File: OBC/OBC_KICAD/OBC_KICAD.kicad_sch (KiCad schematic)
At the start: 0 parts

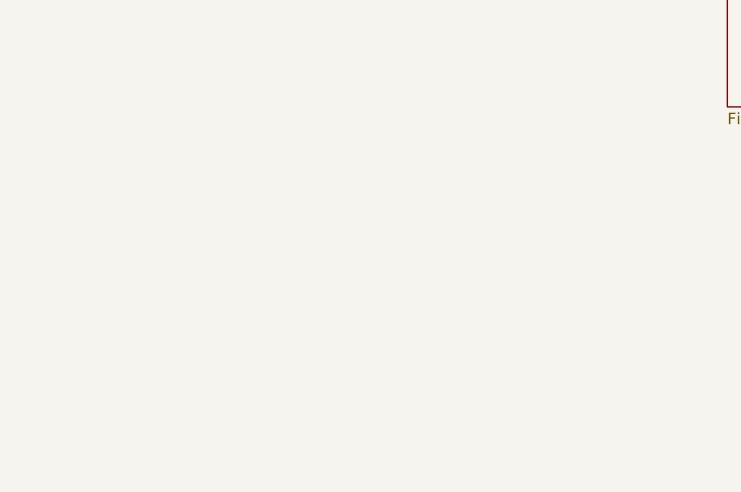
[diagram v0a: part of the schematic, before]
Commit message: Agregar OCP TPS2052BDR y Watchdog STWD100
Agregue un OCP y un WatchDOg ,todo en la HOja con NOmbre Wtachdog.
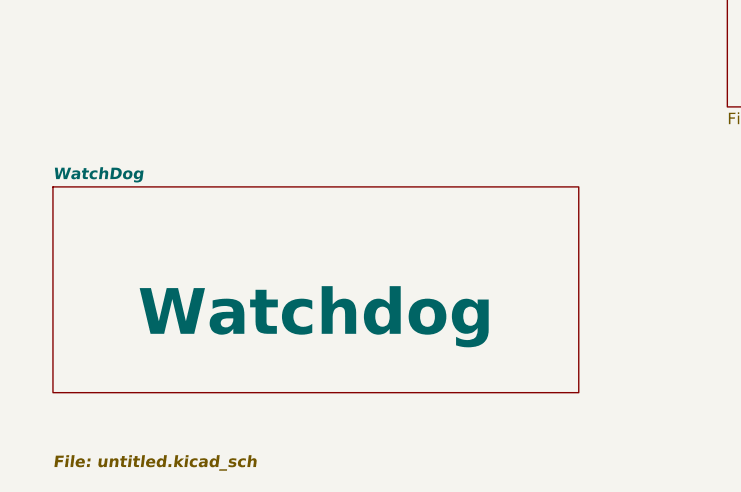
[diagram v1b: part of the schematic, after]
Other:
- added sheet WatchDog (untitled.kicad_sch)
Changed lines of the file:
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@@
+	)
+	(sheet
+		(at 62.23 116.84)
+		(size 58.42 22.86)
+		(exclude_from_sim no)
+		(in_bom yes)
+		(on_board yes)
+		(dnp no)
+		(stroke
+			(width 0.1524)
+			(type solid)
+		)
+		(fill
+			(color 0 0 0 0.0000)
+		)
+		(property "Sheetname" "WatchDog"
+			(at 62.23 116.1284 0)
+			(show_name yes)
+			(effects
+				(font
+					(size 1.27 1.27)
+					(thickness 0.254)
+					(bold yes)
+					(italic yes)
+				)
+				(justify left bottom)
+			)
+		)
+		(property "Sheetfile" "untitled.kicad_sch"
+			(at 62.23 146.6346 0)
+			(show_name yes)
+			(effects
+				(font
+					(size 1.27 1.27)
+					(thickness 0.254)
+					(bold yes)
+					(italic yes)
+				)
+				(justify left top)
+			)
+		)
+		(property "WatchDog" "Watchdog"
+			(at 91.44 130.81 0)
+			(effects
+				(font
+					(size 5.08 5.08)
+					(thickness 1.016)
+					(bold yes)
+				)
+			)
+		)
+		(instances
+			(project "OBC_KICAD"
+				(path "/6db8dc25-5ab8-4f32-8d05-e8d57edb0b6f"
+					(page "4")
+				)
+			)
+		)
 	)
 	(sheet

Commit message: Cirtcuito Completo
Circuito Completo
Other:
- added sheet Pines de Entrada y Salida Al circuito (Pines de Interfaz.kicad_sch)
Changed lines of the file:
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@@
 	(text "JST \nSWD\nUSB"
 		(exclude_from_sim no)
-		(at 166.37 77.47 0)
+		(at 137.16 49.53 0)
 		(effects
 			(font
@@
 	(text "MCU"
 		(exclude_from_sim no)
-		(at 83.058 77.47 0)
+		(at 53.848 49.53 0)
 		(effects
 			(font
@@
 	)
 	(sheet
-		(at 58.42 59.69)
+		(at 29.21 31.75)
 		(size 50.8 30.48)
 		(exclude_from_sim no)
@@
 		)
 		(property "Sheetname" "Microcontrolador"
-			(at 58.42 58.9784 0)
+			(at 29.21 31.0384 0)
 			(effects
 				(font
@@
 		)
 		(property "Sheetfile" "microcontrolador.kicad_sch"
-			(at 58.42 90.7546 0)
+			(at 29.21 62.8146 0)
 			(effects
 				(font
@@
 	)
 	(sheet
-		(at 62.23 116.84)
-		(size 58.42 22.86)
+		(at 19.05 85.09)
+		(size 85.09 26.67)
 		(exclude_from_sim no)
 		(in_bom yes)
@@
 		)
 		(property "Sheetname" "WatchDog"
-			(at 62.23 116.1284 0)
+			(at 19.05 84.3784 0)
 			(show_name yes)
 			(effects
@@
 		)
 		(property "Sheetfile" "untitled.kicad_sch"
-			(at 62.23 146.6346 0)
+			(at 19.05 114.8846 0)
 			(show_name yes)
 			(effects
@@
 			)
 		)
-		(property "WatchDog" "Watchdog"
-			(at 91.44 130.81 0)
+		(property "WatchDog" "    Watchdog n' OCP"
+			(at 48.26 99.06 0)
 			(effects
 				(font
@@
 	)
 	(sheet
-		(at 137.16 44.45)
+		(at 144.78 93.98)
+		(size 106.68 38.1)
+		(exclude_from_sim no)
+		(in_bom yes)
+		(on_board yes)
+		(dnp no)
+		(stroke
+			(width 0.1524)
+			(type solid)
+		)
+		(fill
+			(color 0 0 0 0.0000)
+		)
+		(property "Sheetname" "Pines de Entrada y Salida Al circuito"
+			(at 144.78 93.2684 0)
+			(effects
+				(font
+					(size 1.27 1.27)
+				)
+				(justify left bottom)
+			)
+		)
+		(property "Sheetfile" "Pines de Interfaz.kicad_sch"
+			(at 144.78 128.8546 0)
+			(effects
+				(font
+					(size 1.27 1.27)
+				)
+				(justify left top)
+			)
+		)
+		(property "Field2" "             Pines de Interfaz"
+			(at 180.848 108.966 0)
+			(effects
+				(font
+					(size 4.318 4.318)
+					(thickness 0.8636)
+					(bold yes)
+				)
+			)
+		)
+		(instances
+			(project "OBC_KICAD"
+				(path "/6db8dc25-5ab8-4f32-8d05-e8d57edb0b6f"
+					(page "5")
+				)
+			)
+		)
+	)
+	(sheet
+		(at 107.95 16.51)
 		(size 57.15 63.5)
 		(exclude_from_sim no)
@@
 		)
 		(property "Sheetname" "JST_SWD_USB"
-			(at 137.16 43.7384 0)
+			(at 107.95 15.7984 0)
 			(effects
 				(font
@@
 		)
 		(property "Sheetfile" "JST_Debugger.kicad_sch"
-			(at 137.16 108.5346 0)
-			(effects
-				(font
+			(at 107.95 80.5946 0)
+			(effects
+				(font
